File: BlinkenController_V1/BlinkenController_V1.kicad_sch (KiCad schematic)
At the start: 22 parts, among them J1 Conn_01x02_Socket, J2 Conn_01x08_Socket, J3 Conn_01x03_Socket, J4 4P4C, J5 6P6C, J6 6P6C, U1 Pico, U2 MAX232, U3 TL331

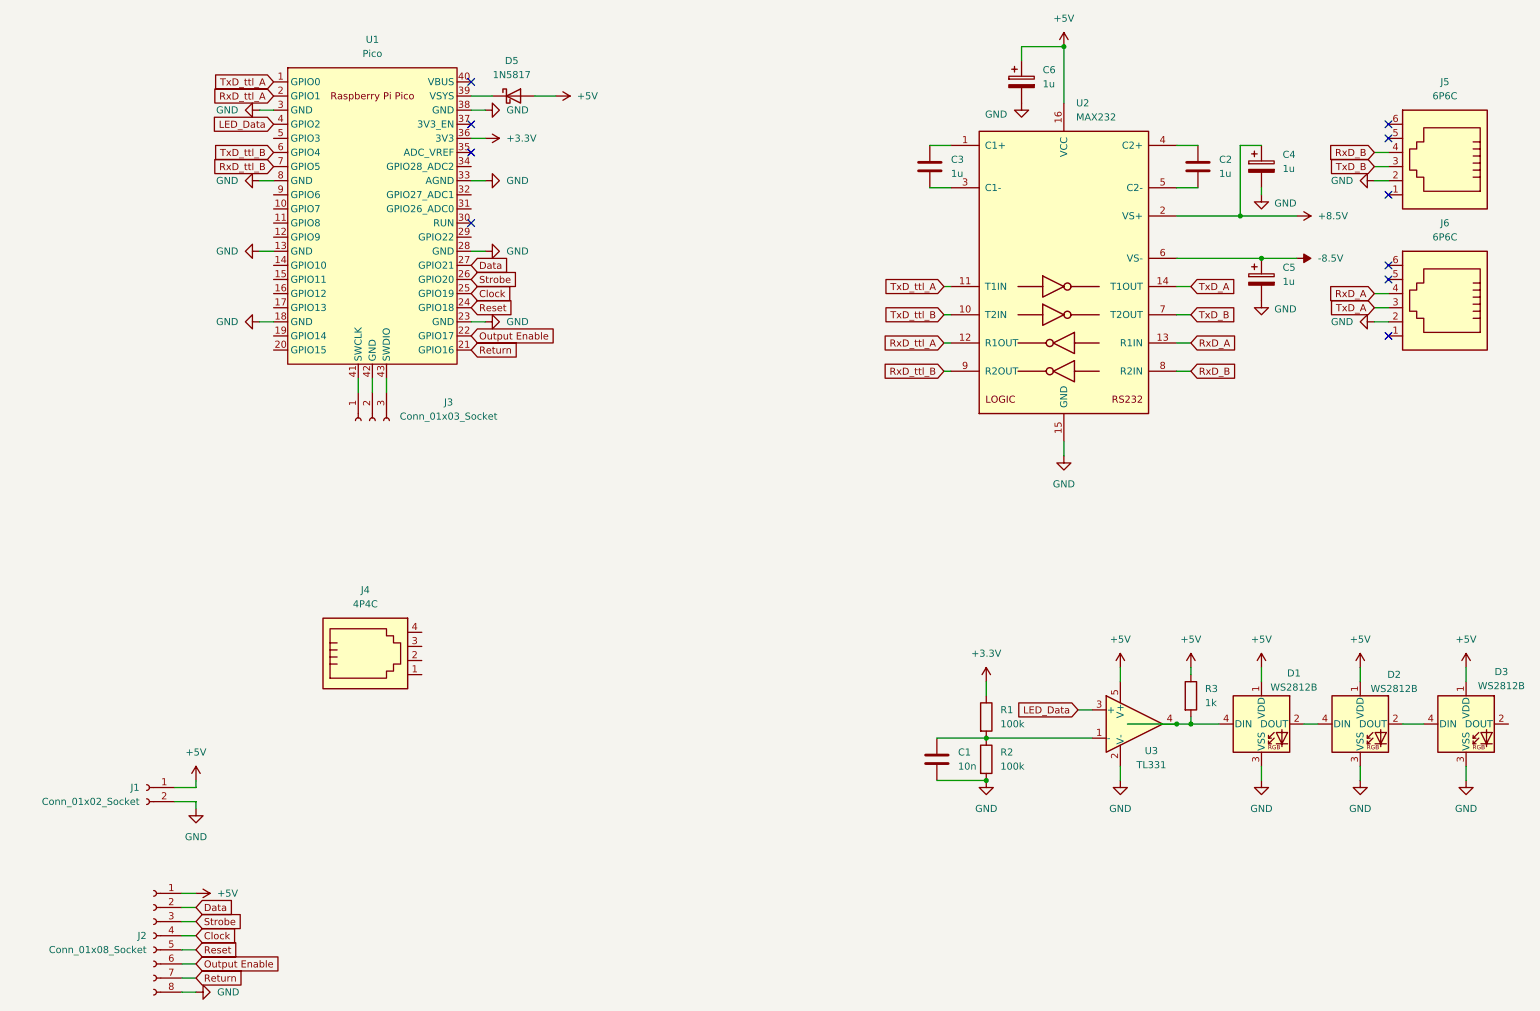
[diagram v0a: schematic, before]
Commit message: Completed board layout of controller
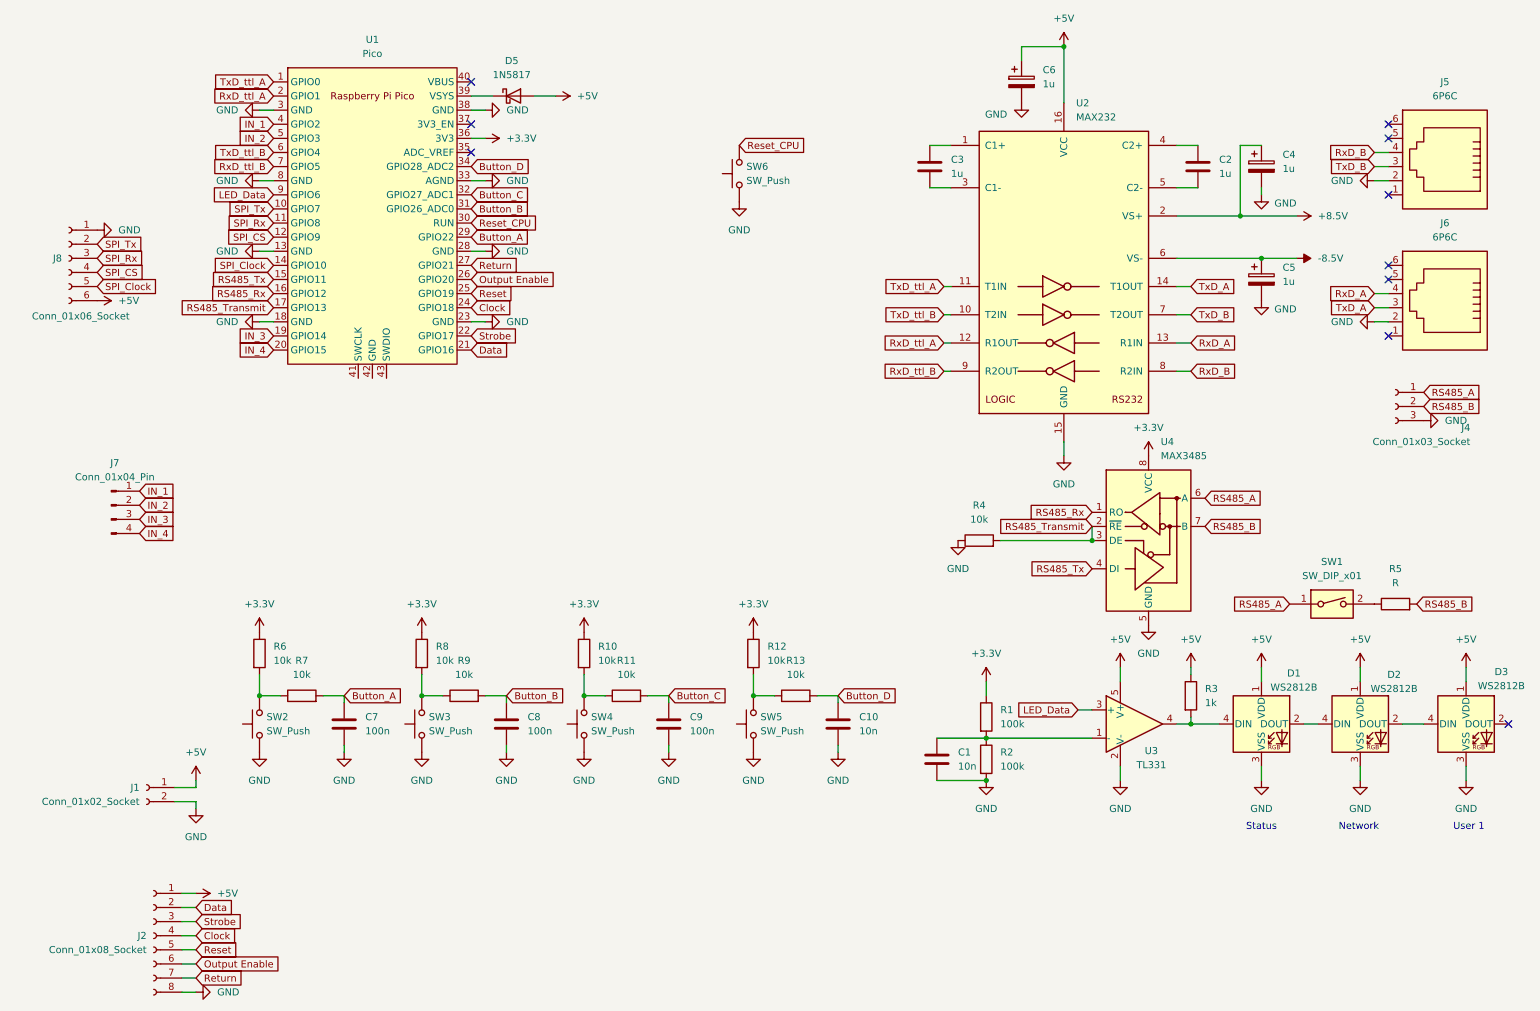
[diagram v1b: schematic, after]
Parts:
- removed J3: Conn_01x03_Socket, symbol Connector:Conn_01x03_Socket
- removed J4: 4P4C, symbol Connector:4P4C
- added C10: 10n, Capacitor_SMD:C_0805_2012Metric_Pad1.18x1.45mm_HandSolder, symbol Device:C
- added C7, C8, C9: 100n, Capacitor_SMD:C_0805_2012Metric_Pad1.18x1.45mm_HandSolder, symbol Device:C
- added J4: Conn_01x03_Socket, Connector_Wago:Wago_734-133_1x03_P3.50mm_Vertical, symbol Connector:Conn_01x03_Socket
- added J7: Conn_01x04_Pin, Connector_Wago:Wago_734-134_1x04_P3.50mm_Vertical, symbol Connector:Conn_01x04_Pin
- added J8: Conn_01x06_Socket, Connector_PinSocket_2.54mm:PinSocket_1x06_P2.54mm_Vertical, symbol Connector:Conn_01x06_Socket
- added R10, R11, R12, R13, R4, R6, R7, R8, R9: 10k, Resistor_SMD:R_0805_2012Metric_Pad1.20x1.40mm_HandSolder, symbol Device:R
- added R5: R, Resistor_SMD:R_0805_2012Metric_Pad1.20x1.40mm_HandSolder, symbol Device:R
- added SW1: SW_DIP_x01, Button_Switch_THT:SW_Slide-03_Wuerth-WS-SLTV_10x2.5x6.4_P2.54mm, symbol Switch:SW_DIP_x01
- added SW2, SW3, SW4, SW5, SW6: SW_Push, Button_Switch_SMD:SW_SPST_PTS810, symbol Switch:SW_Push
- added U4: MAX3485, Package_SO:SOIC-8_3.9x4.9mm_P1.27mm, symbol Interface_UART:MAX3485
- C1: footprint (none) -> Capacitor_SMD:C_0805_2012Metric_Pad1.18x1.45mm_HandSolder
- C2: footprint (none) -> Capacitor_THT:C_Radial_D6.3mm_H7.0mm_P2.50mm
- C3, C4, C5, C6: footprint (none) -> Capacitor_THT:C_Radial_D6.3mm_H5.0mm_P2.50mm
- J1: footprint (none) -> Connector_Wago:Wago_734-132_1x02_P3.50mm_Vertical
- J2: footprint (none) -> Connector_PinSocket_2.54mm:PinSocket_1x08_P2.54mm_Horizontal
- J5, J6: footprint (none) -> Connector_RJ:RJ12_Amphenol_54601-x06_Horizontal
- R1, R2, R3: footprint (none) -> Resistor_SMD:R_0805_2012Metric_Pad1.20x1.40mm_HandSolder
- U1: footprint RPi_Pico:RPi_Pico_SMD_TH -> Module:RaspberryPi_Pico_W_SMD
- U2: footprint (none) -> Package_DIP:DIP-16_W7.62mm_LongPads
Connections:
- net +3.3V: now also R10.1, R12.1, R6.1, R8.1, U4.8 (VCC)
- net +5V: now also J8.6 (Pin_6)
- net Clock: now also U1.24 (GPIO18); no longer U1.25 (GPIO19)
- net Data: now also U1.21 (GPIO16); no longer U1.27 (GPIO21)
- net GND: now also C10.2, C7.2, C8.2, C9.2, J4.3 (Pin_3), J8.1 (Pin_1), R4.1, SW2.1, SW3.1, SW4.1, SW5.1, SW6.1, U4.5 (GND)
- net LED_Data: now also U1.9 (GPIO6); no longer U1.4 (GPIO2)
- net Output Enable: now also U1.26 (GPIO20); no longer U1.22 (GPIO17)
- net Reset: now also U1.25 (GPIO19); no longer U1.24 (GPIO18)
- net Return: now also U1.27 (GPIO21); no longer U1.21 (GPIO16)
- net Strobe: now also U1.22 (GPIO17); no longer U1.26 (GPIO20)
- net SPI_Tx: now reaches U1.10 (GPIO7)
- net SPI_Tx: now also J8.2 (Pin_2)
- net SPI_Rx: now reaches U1.11 (GPIO8)
- net SPI_Rx: now also J8.3 (Pin_3)
- net SPI_CS: now reaches U1.12 (GPIO9)
- net SPI_CS: now also J8.4 (Pin_4)
- net SPI_Clock: now reaches U1.14 (GPIO10)
- net SPI_Clock: now also J8.5 (Pin_5)
- net RS485_Tx: now reaches U1.15 (GPIO11)
- net RS485_Tx: now also U4.4 (DI)
- net RS485_Rx: now reaches U1.16 (GPIO12)
- net RS485_Rx: now also U4.1 (RO)
- net RS485_Transmit: now reaches U1.17 (GPIO13)
- net RS485_Transmit: now also R4.2, U4.2 (~{RE}), U4.3 (DE)
- net IN_3: now reaches U1.19 (GPIO14)
- net IN_3: now also J7.3 (Pin_3)
- net IN_4: now reaches U1.20 (GPIO15)
- net IN_4: now also J7.4 (Pin_4)
- net Button_A: now reaches U1.29 (GPIO22)
- net Button_A: now also C7.1, R7.2
- net Reset_CPU: now reaches U1.30 (RUN)
- net Reset_CPU: now also SW6.2
- net Button_B: now reaches U1.31 (GPIO26_ADC0)
- net Button_B: now also C8.1, R9.2
- net Button_C: now reaches U1.32 (GPIO27_ADC1)
- net Button_C: now also C9.1, R11.2
- net Button_D: now reaches U1.34 (GPIO28_ADC2)
- net Button_D: now also C10.1, R13.2
- net IN_2: now reaches U1.5 (GPIO3)
- net IN_2: now also J7.2 (Pin_2)
- new net: R12.2, R13.1, SW5.2
- new net: R8.2, R9.1, SW3.2
- new net: R10.2, R11.1, SW4.2
- new net: R6.2, R7.1, SW2.2
- new net: R5.1, SW1.2
- new net IN_1: J7.1 (Pin_1), U1.4 (GPIO2)
- new net RS485_A: J4.1 (Pin_1), SW1.1, U4.6 (A)
- new net RS485_B: J4.2 (Pin_2), R5.2, U4.7 (B)
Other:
- note added: "Network"
- note added: "Status"
- note added: "User 1"

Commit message: Improved board density
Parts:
- C2: footprint Capacitor_THT:C_Radial_D6.3mm_H7.0mm_P2.50mm -> Capacitor_THT:C_Disc_D5.0mm_W2.5mm_P5.00mm
- C3: footprint Capacitor_THT:C_Radial_D6.3mm_H5.0mm_P2.50mm -> Capacitor_THT:C_Disc_D5.0mm_W2.5mm_P5.00mm
- J1: footprint Connector_Wago:Wago_734-132_1x02_P3.50mm_Vertical -> Connector_Phoenix_MSTB:PhoenixContact_MSTBVA_2,5_2-G_1x02_P5.00mm_Vertical
- J4: footprint Connector_Wago:Wago_734-133_1x03_P3.50mm_Vertical -> Connector_Phoenix_MSTB:PhoenixContact_MSTBVA_2,5_3-G_1x03_P5.00mm_Vertical
- J7: footprint Connector_Wago:Wago_734-134_1x04_P3.50mm_Vertical -> Connector_Phoenix_MSTB:PhoenixContact_MSTBVA_2,5_4-G_1x04_P5.00mm_Vertical
- SW2, SW3, SW4, SW5, SW6: footprint Button_Switch_SMD:SW_SPST_PTS810 -> Button_Switch_SMD:SW_Tactile_SPST_NO_Straight_CK_PTS636Sx25SMTRLFS
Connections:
- net RS485_Rx: now also U1.17 (GPIO13); no longer U1.16 (GPIO12)
- net RS485_Transmit: now also U1.16 (GPIO12); no longer U1.17 (GPIO13)
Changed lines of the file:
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@@
 	(global_label "RS485_Transmit"
 		(shape input)
-		(at 58.42 68.58 180)
+		(at 58.42 66.04 180)
 		(fields_autoplaced yes)
 		(effects
@@
 		)
 		(property "Intersheetrefs" "${INTERSHEET_REFS}"
-			(at 40.2555 68.58 0)
+			(at 40.2555 66.04 0)
 			(effects
 				(font
@@
 	(global_label "RS485_Rx"
 		(shape input)
-		(at 58.42 66.04 180)
+		(at 58.42 68.58 180)
 		(fields_autoplaced yes)
 		(effects
@@
 		)
 		(property "Intersheetrefs" "${INTERSHEET_REFS}"
-			(at 46.0611 66.04 0)
+			(at 46.0611 68.58 0)
 			(effects
 				(font
@@
 			)
 		)
-		(property "Footprint" "Button_Switch_SMD:SW_SPST_PTS810"
+		(property "Footprint" "Button_Switch_SMD:SW_Tactile_SPST_NO_Straight_CK_PTS636Sx25SMTRLFS"
 			(at 139.7 143.51 0)
 			(effects
@@
 			)
 		)
-		(property "Footprint" "Button_Switch_SMD:SW_SPST_PTS810"
+		(property "Footprint" "Button_Switch_SMD:SW_Tactile_SPST_NO_Straight_CK_PTS636Sx25SMTRLFS"
 			(at 50.8 143.51 0)
 			(effects
@@
 			)
 		)
-		(property "Footprint" "Connector_Wago:Wago_734-133_1x03_P3.50mm_Vertical"
+		(property "Footprint" "Connector_Phoenix_MSTB:PhoenixContact_MSTBVA_2,5_3-G_1x03_P5.00mm_Vertical"
 			(at 260.35 86.36 0)
 			(effects
@@
 			)
 		)
-		(property "Footprint" "Button_Switch_SMD:SW_SPST_PTS810"
+		(property "Footprint" "Button_Switch_SMD:SW_Tactile_SPST_NO_Straight_CK_PTS636Sx25SMTRLFS"
 			(at 80.01 143.51 0)
 			(effects
@@
 			)
 		)
-		(property "Footprint" "Capacitor_THT:C_Radial_D6.3mm_H7.0mm_P2.50mm"
+		(property "Footprint" "Capacitor_THT:C_Disc_D5.0mm_W2.5mm_P5.00mm"
 			(at 225.7552 46.99 0)
 			(effects
@@
 			)
 		)
-		(property "Footprint" "Connector_Wago:Wago_734-132_1x02_P3.50mm_Vertical"
+		(property "Footprint" "Connector_Phoenix_MSTB:PhoenixContact_MSTBVA_2,5_2-G_1x02_P5.00mm_Vertical"
 			(at 35.56 154.94 0)
 			(effects
@@
 			)
 		)
-		(property "Footprint" "Capacitor_THT:C_Radial_D6.3mm_H5.0mm_P2.50mm"
+		(property "Footprint" "Capacitor_THT:C_Disc_D5.0mm_W2.5mm_P5.00mm"
 			(at 177.4952 46.99 0)
 			(effects
@@
 			)
 		)
-		(property "Footprint" "Button_Switch_SMD:SW_SPST_PTS810"
+		(property "Footprint" "Button_Switch_SMD:SW_Tactile_SPST_NO_Straight_CK_PTS636Sx25SMTRLFS"
 			(at 109.22 143.51 0)
 			(effects
@@
 			)
 		)
-		(property "Footprint" "Connector_Wago:Wago_734-134_1x04_P3.50mm_Vertical"
+		(property "Footprint" "Connector_Phoenix_MSTB:PhoenixContact_MSTBVA_2,5_4-G_1x04_P5.00mm_Vertical"
 			(at 29.21 104.14 0)
 			(effects
@@
 			)
 		)
-		(property "Footprint" "Button_Switch_SMD:SW_SPST_PTS810"
+		(property "Footprint" "Button_Switch_SMD:SW_Tactile_SPST_NO_Straight_CK_PTS636Sx25SMTRLFS"
 			(at 137.16 44.45 0)
 			(effects

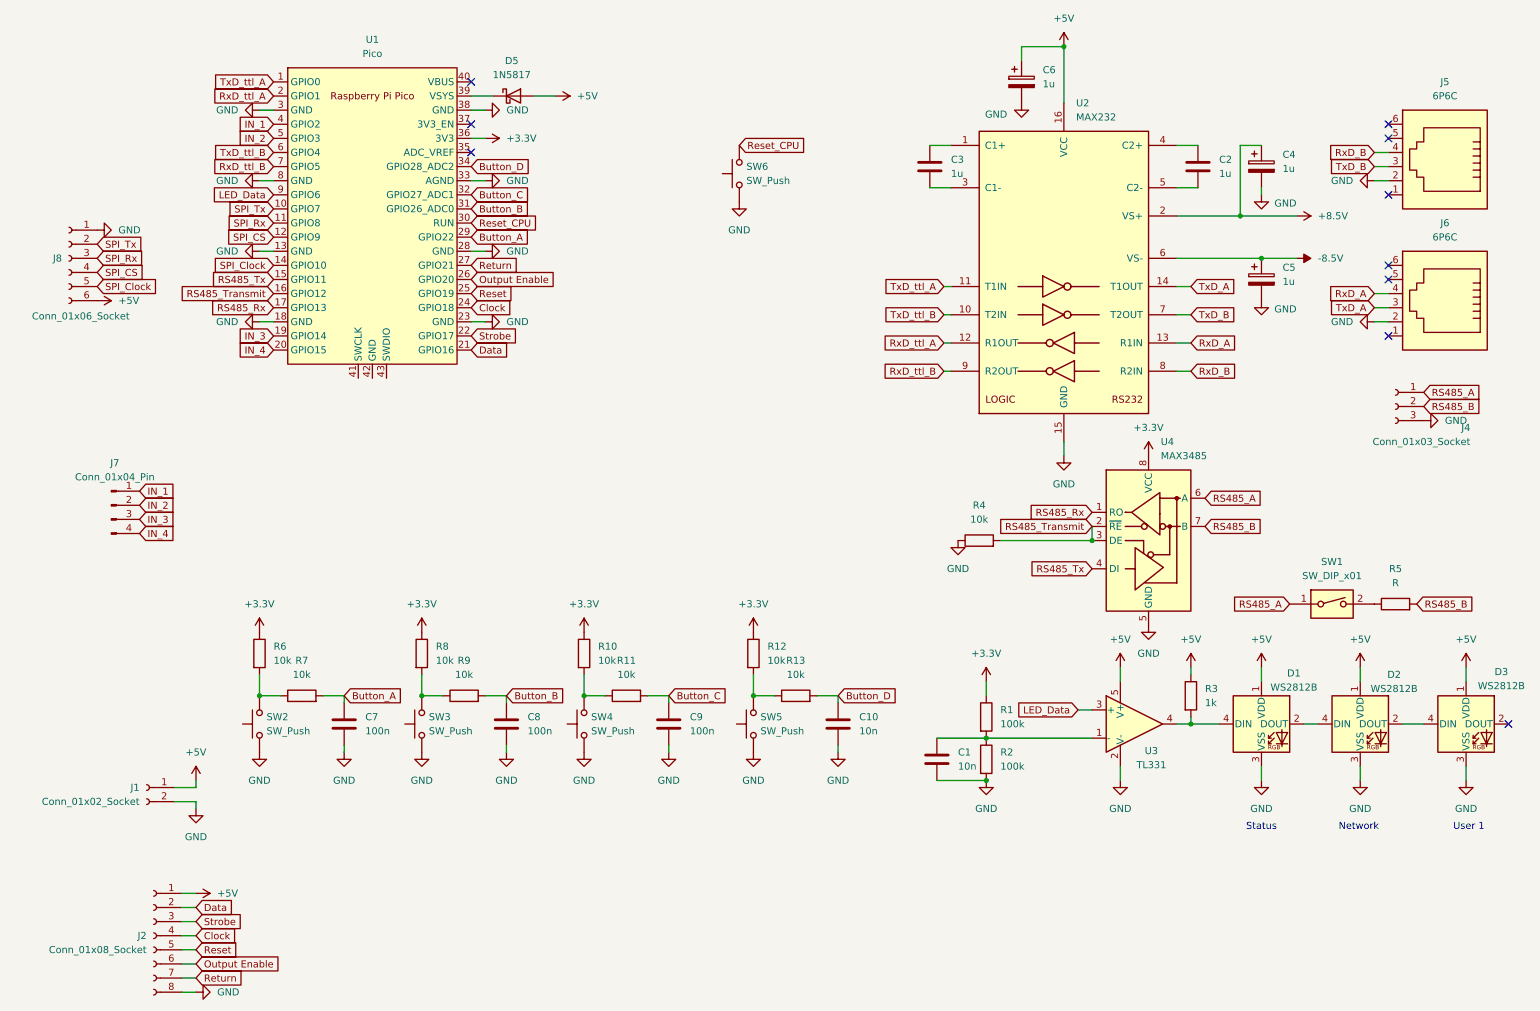
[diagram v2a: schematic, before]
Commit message: Finished PCB design and added Level Shifter
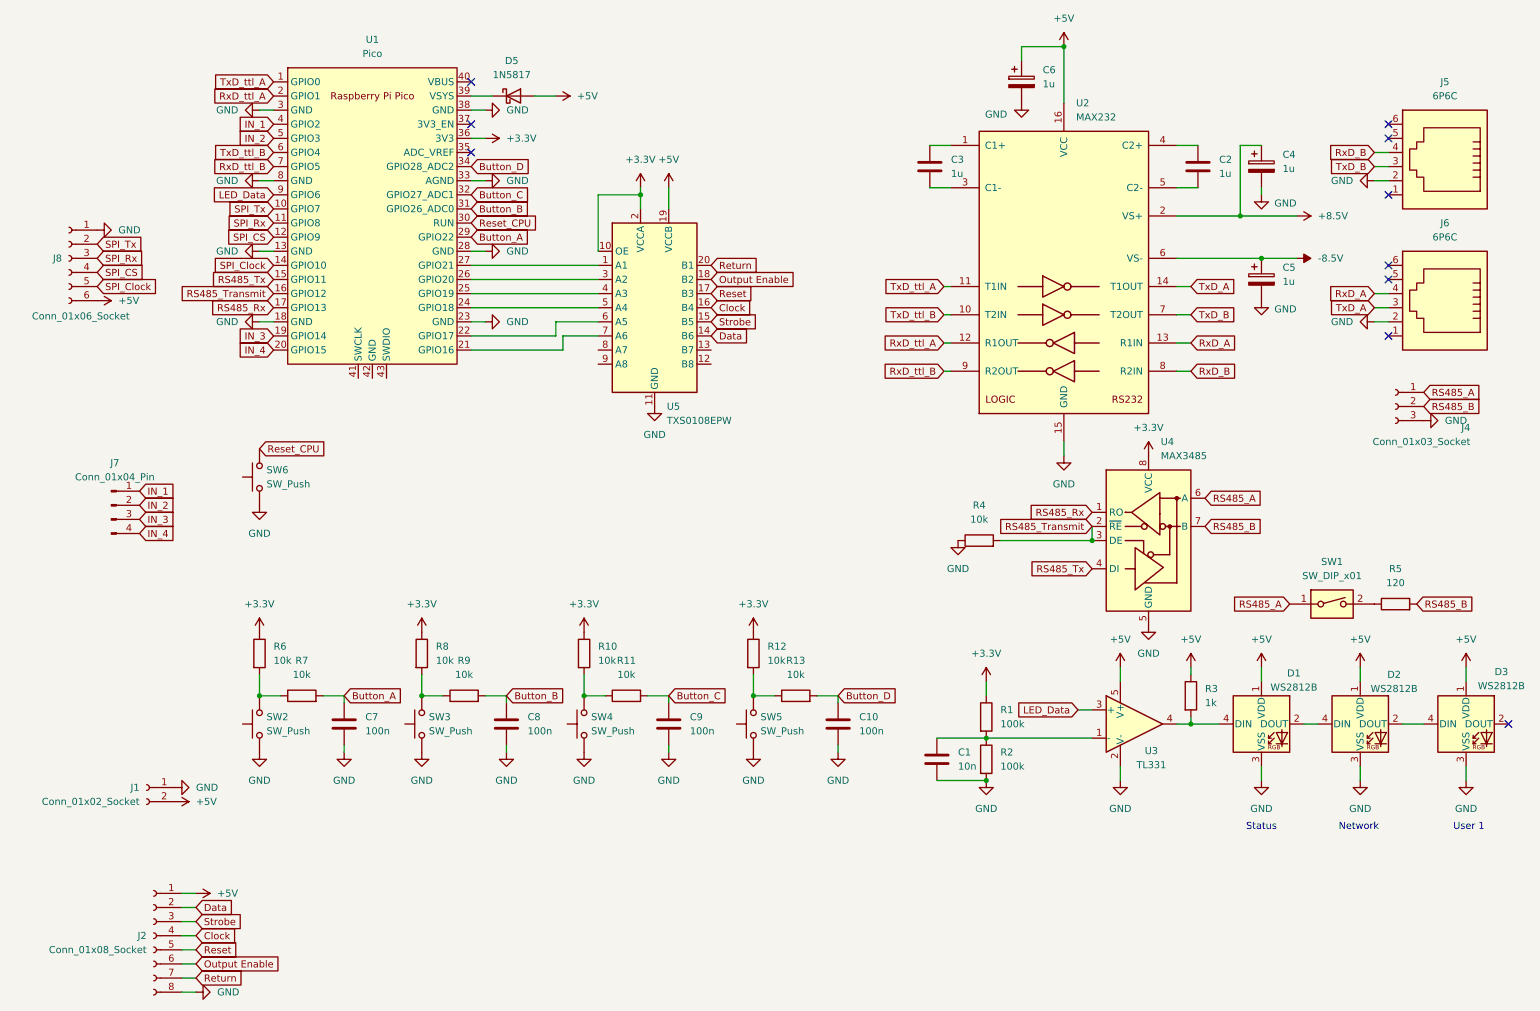
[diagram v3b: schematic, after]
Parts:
- added U5: TXS0108EPW, Package_SO:TSSOP-20_4.4x6.5mm_P0.65mm, symbol Logic_LevelTranslator:TXS0108EPW
- C10: value 10n -> 100n
- R5: value R -> 120
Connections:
- net +3.3V: now also U5.10 (OE), U5.2 (VCCA)
- net +5V: now also J1.2 (Pin_2), U5.19 (VCCB); no longer J1.1 (Pin_1)
- net Clock: now also U5.16 (B4); no longer U1.24 (GPIO18)
- net Data: now also U5.14 (B6); no longer U1.21 (GPIO16)
- net GND: now also J1.1 (Pin_1), U5.11 (GND); no longer J1.2 (Pin_2)
- net Output Enable: now also U5.18 (B2); no longer U1.26 (GPIO20)
- net Reset: now also U5.17 (B3); no longer U1.25 (GPIO19)
- net Return: now also U5.20 (B1); no longer U1.27 (GPIO21)
- net Strobe: now also U5.15 (B5); no longer U1.22 (GPIO17)
- new net: U1.21 (GPIO16), U5.7 (A6)
- new net: U1.22 (GPIO17), U5.6 (A5)
- new net: U1.24 (GPIO18), U5.5 (A4)
- new net: U1.25 (GPIO19), U5.4 (A3)
- new net: U1.26 (GPIO20), U5.3 (A2)
- new net: U1.27 (GPIO21), U5.1 (A1)
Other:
- moved on the sheet: SW6
